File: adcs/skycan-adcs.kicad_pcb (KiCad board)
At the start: 2 copper layers, 50 x 50 mm, 43 parts, among them J1 DF9_25P_1V_PLUG, J2 DF9_25P_1V_SOCKET, J3 DF9_25P_1V_PLUG, J4 DF9_25P_1V_SOCKET, U1 TPS63060, U2 BQ27210, U3 MICRO-B_USB, U4 MCP73831, U5 SWITCH-DPDT

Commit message: adcs routing inprogress
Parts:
- removed BT2: LiPo, PINHEAD1-2
- removed C11, C12: 100nF, SM0402_c
- removed C13, C14: 4.7uF, SM0805
- removed D1: LED, LED-0603
- removed L1: 1uH, COILCRAFT-XFL4020
- removed R10: 2R, SM0402_r
- BT1: value 3x1.5V AAA -> BATTERY; footprint BATTERY-HOLDER-KEYSTONE-2479 -> COINCELL3001; moved to F.Cu
- C1: value 10uF -> 100nF; footprint SM0805 -> SM0402_c
- C10: value 100nF -> 4.7uF; footprint SM0402_c -> SM0603_Capa
- C4: value 10pF -> 100nF
- C5: value 22uF -> 100nF; footprint SM0805 -> SM0402_c
- C6: value 22uF -> 10uF
- C7: value 22uF -> 10uF; footprint SM0805 -> SM0603_Resistor
- C9: value 100nF -> 220nF
- R1, R7: value 1M -> 4.7k
- R2: value 168k -> 4.7k
- R3: value 100k -> 4.7k
- R4: value 1k -> 4.7k
- R5: value 10k -> 330R
- R6: value 1M -> 330R
- R8: value 0.02R -> 4.7k; footprint SM0603_Resistor -> SM0402_r
- R9: value 470R -> 4.7k
- U1: value TPS63060 -> ADT7310; footprint S-PWSON-N10 -> SO8N
- U2: value BQ27210 -> MPL3115A2; footprint S-PVSON-N10 -> LGA8
- U3: value MICRO-B_USB -> LSM303DLHC; footprint MICRO-B_USB -> LGA14L
- U4: value MCP73831 -> MAX-7C; footprint SOT23-5 -> MAX7
- U5: value SWITCH-DPDT -> UFL; footprint MCLSS22P-SWITCH-DPDT -> UFL
- moved R9 45.2 mm to (89.4, 102.5), turned to 180 degrees
- moved G*** 43.4 mm to (168.1, 98.3)
- moved VAL 37.7 mm to (159.8, 79.0)
- moved R8 31.9 mm to (96.1, 102.0), turned to 90 degrees
- moved R7 29.6 mm to (97.3, 102.0), turned to 90 degrees
- moved C5 24.0 mm to (111.8, 100.5)
- moved C1 21.9 mm to (122.0, 107.2), turned to 270 degrees
- moved C6 21.5 mm to (111.9, 102.1)
- moved U3 21.4 mm to (118.7, 117.1), turned to 180 degrees
- moved R3 20.7 mm to (116.8, 110.7), turned to 270 degrees
- moved C3 20.6 mm to (118.7, 103.8), turned to 180 degrees
- moved C2 19.4 mm to (123.8, 107.2), turned to 270 degrees
- moved BT1 17.6 mm to (125.0, 97.4), turned to 0 degrees
- moved R2 15.3 mm to (118.1, 110.7), turned to 270 degrees
- moved U1 14.4 mm to (130.8, 107.1)
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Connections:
- BT1 pad 1: /VBAT -> N-0000022
- BT1 pad 2: GNDPWR -> GND
- C1 pad 1: /VIN -> +3.3V
- C10 pad 1: N-0000010 -> N-0000028
- C10 pad 2: GNDPWR -> GND
- C2 pad 1: /VIN -> +3.3V
- C3 pad 1: N-000008 -> N-0000029
- C4 pad 1: N-0000050 -> +3.3V
- C8 pad 1: N-000009 -> +3.3V
- C8 pad 2: GNDPWR -> GND
- C9 pad 1: N-0000012 -> N-0000026
- C9 pad 2: GNDPWR -> N-0000031
- R1 pad 1: +3.3V -> P1.3
- R1 pad 2: N-0000050 -> +3.3V
- R2 pad 1: N-0000050 -> P1.6
- R2 pad 2: GND -> +3.3V
- R3 pad 1: +3.3V -> P1.7
- R3 pad 2: PGOOD -> +3.3V
- R4 pad 1: N-000009 -> P1.0
- R4 pad 2: /VBAT -> +3.3V
- R5 pad 1: N-0000010 -> N-000004
- R5 pad 2: /VBAT -> RXA1
- R6 pad 1: N-0000052 -> N-000006
- R6 pad 2: GNDPWR -> TXA1
- R7 pad 1: N-0000013 -> P1.5
- R7 pad 2: GND -> +3.3V
- R8 pad 1: GND -> P1.4
- R8 pad 2: GNDPWR -> +3.3V
- R9 pad 1: N-000001 -> P1.2
- R9 pad 2: N-000002 -> +3.3V
- U1 pad 1: N-0000047 -> CLKB1
- U1 pad 2: /VIN -> SOMIB1
- U1 pad 3: /VIN -> SIMOB1
- U1 pad 4: GND -> P4.6
- U1 pad 5: PGOOD -> P1.3
- U1 pad 6: N-000008 -> (no net)
- U1 pad 8: N-0000050 -> +3.3V
- U2 pad 1: N-0000012 -> +3.3V
- U2 pad 2: N-000009 -> N-0000029
- U2 pad 3: GNDPWR -> GND
- U2 pad 4: SCLB0 -> +3.3V
- U2 pad 5: SDAB0 -> P1.7
- U2 pad 6: N-0000010 -> P1.6
- U2 pad 7: N-0000013 -> SDAB0
- U2 pad 8: N-0000052 -> SCLB0
- U3 pad 1: N-000004 -> +3.3V
- U3 pad 2: N-0000029 -> SCLB0
- U3 pad 3: N-0000030 -> SDAB0
- U3 pad 4: N-0000031 -> P1.5
- U3 pad 5: GND -> P1.4
- U4 pad 1: N-000001 -> GND
- U4 pad 2: GND -> N-000004
- U4 pad 3: /VBAT -> N-000006
- U4 pad 4: N-000004 -> P1.1
- U4 pad 5: N-0000028 -> P1.0
- U5 pad 1: /VIN -> N-0000018
- U5 pad 2: /VIN -> GND
- U5 pad 3: /VBAT -> GND
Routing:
- net GND: track 600.8 -> 59.8 mm, vias 274 -> 21
- net +3.3V: track 182.7 -> 66.1 mm
- net GNDPWR: track 69.3 -> 0.00 mm, vias 18 -> 0
- net /VBAT: track 58.2 -> 0.00 mm, vias 2 -> 0
- net P1.1: track 3.01 -> 39.4 mm
- net P1.0: track 3.02 -> 35.2 mm
- net P1.6: track 3.05 -> 31.0 mm
- net P1.7: track 3.04 -> 27.3 mm
- net SCLB0: track 29.8 -> 54.0 mm
- net TXA1: track 2.19 -> 23.4 mm, vias 1 -> 3
- net RXA1: track 2.17 -> 21.5 mm
- net SDAB0: track 32.4 -> 51.3 mm, vias 5 -> 3
- net /VIN: track 16.3 -> 0.00 mm
- net P4.6: track 2.17 -> 18.2 mm
- net N-000004: track 16.5 -> 1.89 mm
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- removed copper zone on F.Cu, net /VBAT
- removed copper zone on B.Cu, net GNDPWR
- removed copper zone on F.Cu, net GNDPWR
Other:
- board text removed: "+"
- board text removed: "-"
- board text removed: "0"
- board text removed: "1"

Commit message: punch of stuff routed in adcs
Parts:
- moved R1 24.6 mm to (103.3, 116.2), turned to 180 degrees
- moved R9 20.3 mm to (103.3, 117.3)
- moved R2 15.0 mm to (103.3, 112.8), turned to 180 degrees
- moved R8 14.9 mm to (103.3, 115.1), turned to 180 degrees
- moved R3 13.6 mm to (103.3, 111.6), turned to 180 degrees
- moved R7 13.3 mm to (103.3, 113.9), turned to 180 degrees
- moved C5 5.74 mm to (116.5, 103.8)
- moved C6 3.81 mm to (115.7, 102.0)
- moved R4 1.40 mm to (125.6, 121.3)
- moved C1 0.65 mm to (122.2, 106.6)
- moved C2 0.13 mm to (124.0, 107.2)
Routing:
- net P1.6: track 31.0 -> 5.48 mm
- net P1.7: track 27.3 -> 6.12 mm
- net P1.0: track 35.2 -> 27.4 mm
- net +3.3V: track 66.1 -> 72.6 mm
- net P1.1: track 39.4 -> 35.6 mm
- net P1.2: track 16.3 -> 18.8 mm
- net P1.3: track 3.09 -> 5.47 mm
- net P1.5: track 15.5 -> 17.9 mm
- net P1.4: track 14.5 -> 16.8 mm
- net N-0000029: track 0.00 -> 1.97 mm
- net N-0000026: track 0.00 -> 1.94 mm
- net N-0000031: track 0.00 -> 1.90 mm

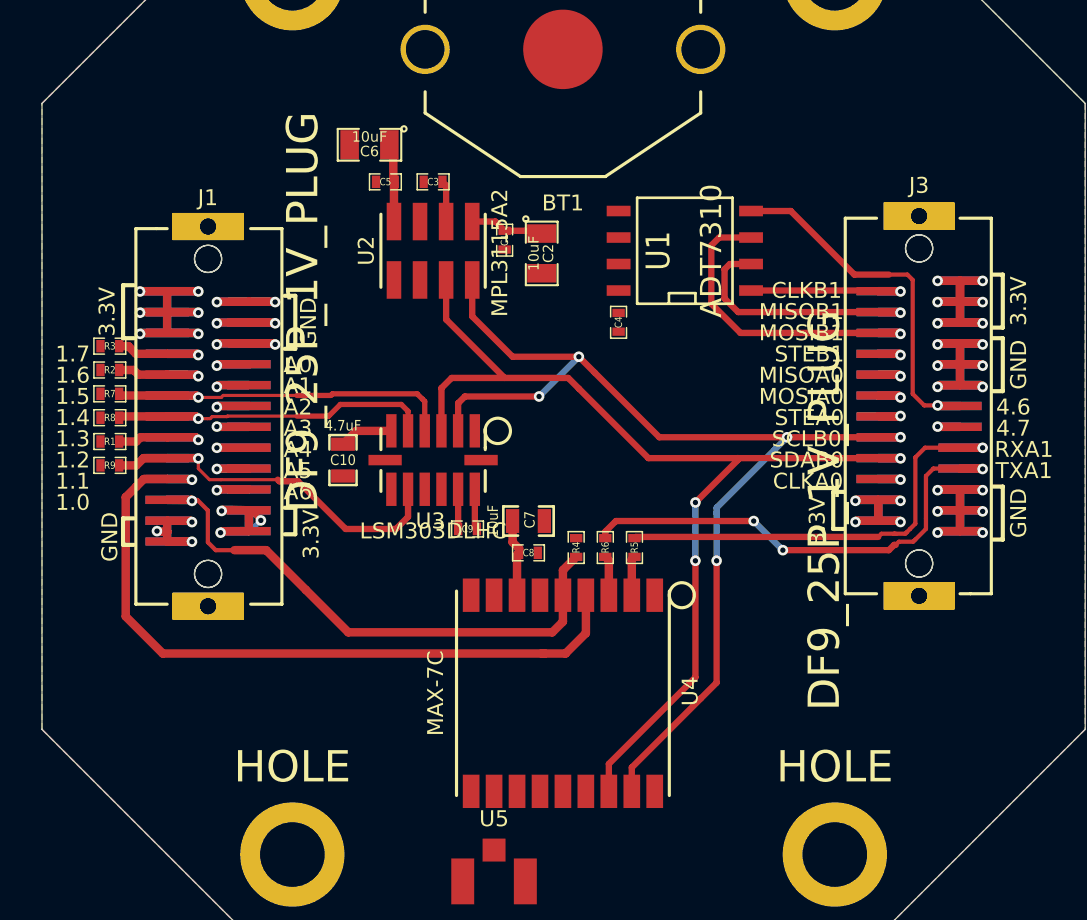
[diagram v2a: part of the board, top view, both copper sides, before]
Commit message: signals routed
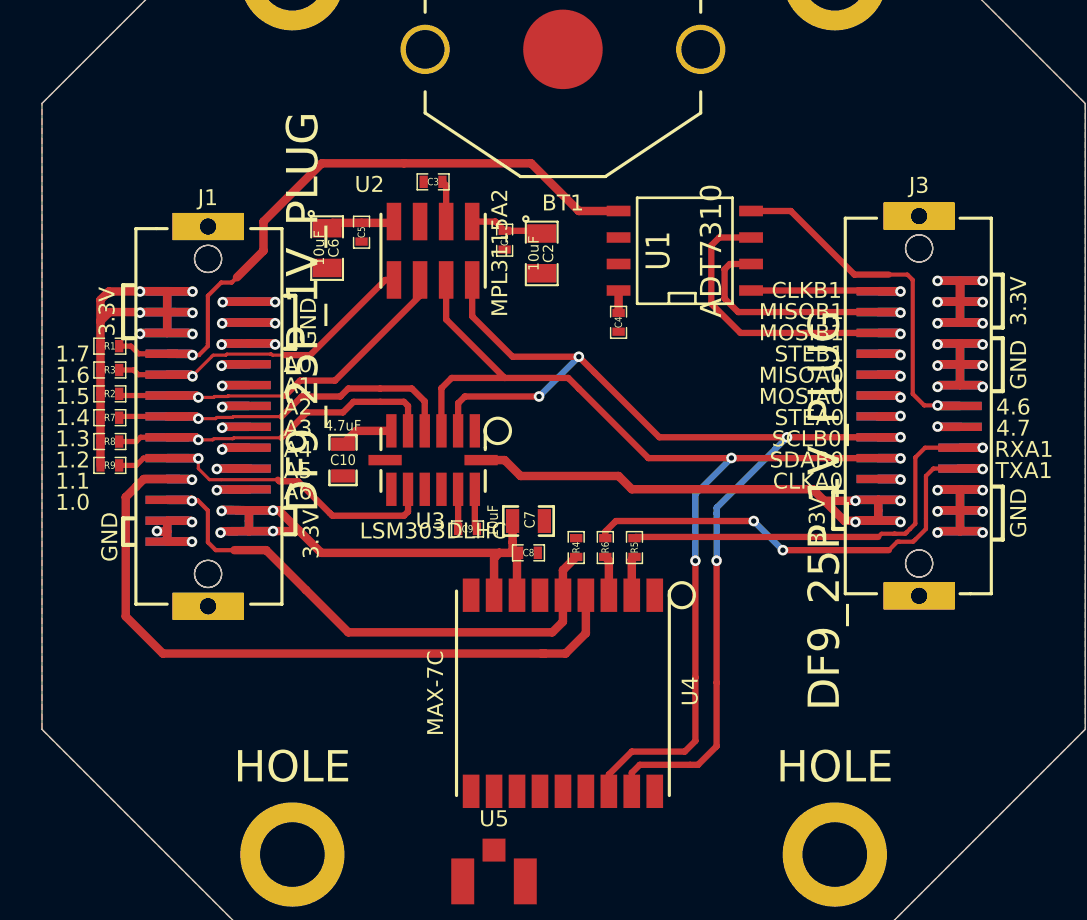
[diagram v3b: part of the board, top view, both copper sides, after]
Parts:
- moved C6 5.35 mm to (113.7, 106.9), turned to 270 degrees
- moved R1 4.57 mm to (103.3, 111.6)
- moved C5 2.67 mm to (115.3, 106.2), turned to 270 degrees
- moved R2 1.14 mm to (103.3, 113.9)
- moved R3 1.14 mm to (103.3, 112.8)
- moved R7 1.14 mm to (103.3, 115.1)
- moved R8 1.14 mm to (103.3, 116.2)
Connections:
- R1 pad 1: P1.3 -> P1.7
- R2 pad 1: P1.6 -> P1.5
- R3 pad 1: P1.7 -> P1.6
- R7 pad 1: P1.5 -> P1.4
- R8 pad 1: P1.4 -> P1.3
- U1 pad 5: P1.3 -> P1.7
- U2 pad 5: P1.7 -> P1.6
- U2 pad 6: P1.6 -> P1.5
- U3 pad 4: P1.5 -> P1.4
- U3 pad 5: P1.4 -> P1.3
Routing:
- net +3.3V: track 72.6 -> 123.9 mm, vias 19 -> 20
- net P1.7: track 6.12 -> 32.4 mm
- net P1.3: track 5.47 -> 17.6 mm
- net P1.6: track 5.48 -> 17.2 mm
- net P1.4: track 16.8 -> 18.5 mm
- net SCLB0: track 54.0 -> 55.7 mm
- net GND: track 59.8 -> 58.2 mm
- net SDAB0: track 51.3 -> 52.7 mm
- net P1.5: track 17.9 -> 18.8 mm
- net P1.2: track 18.8 -> 18.1 mm
- net A1: track 3.15 -> 2.60 mm
- net A2: track 3.12 -> 2.61 mm

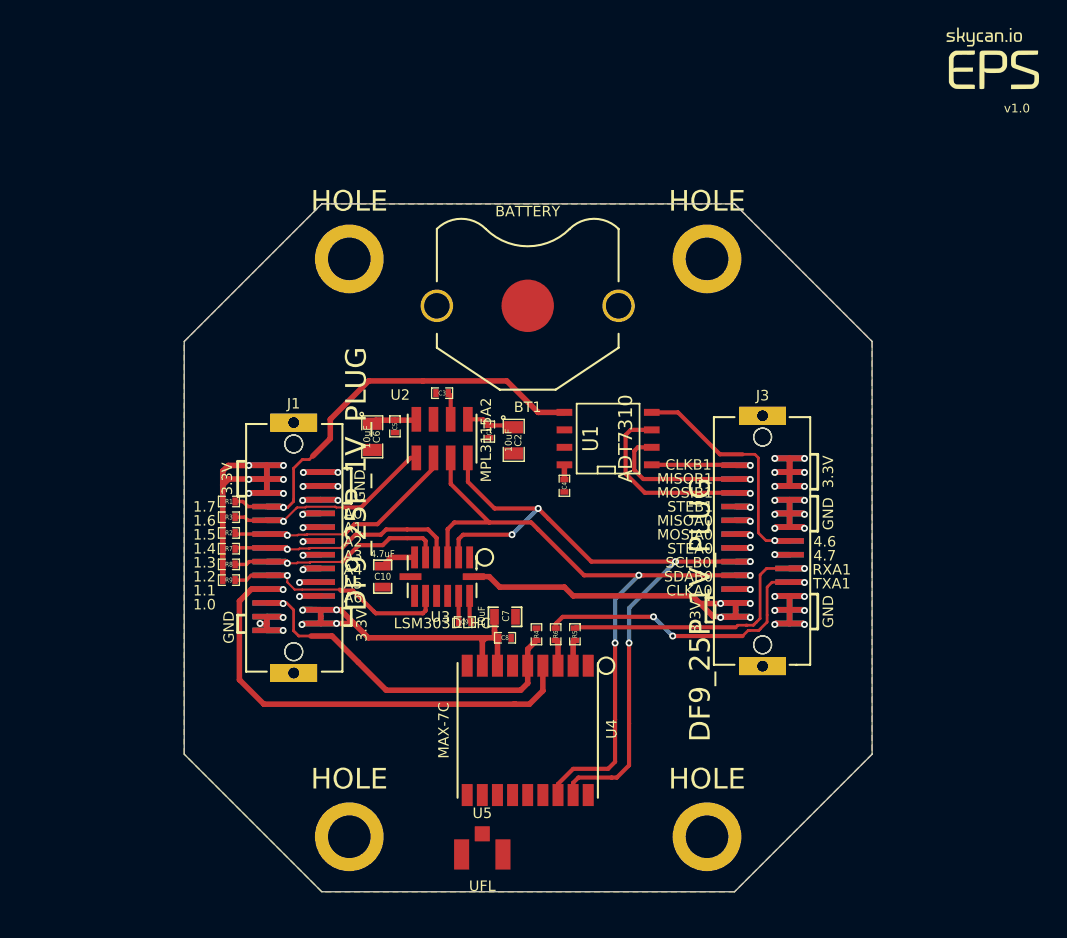
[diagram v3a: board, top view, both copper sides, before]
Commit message: finish adcs routing
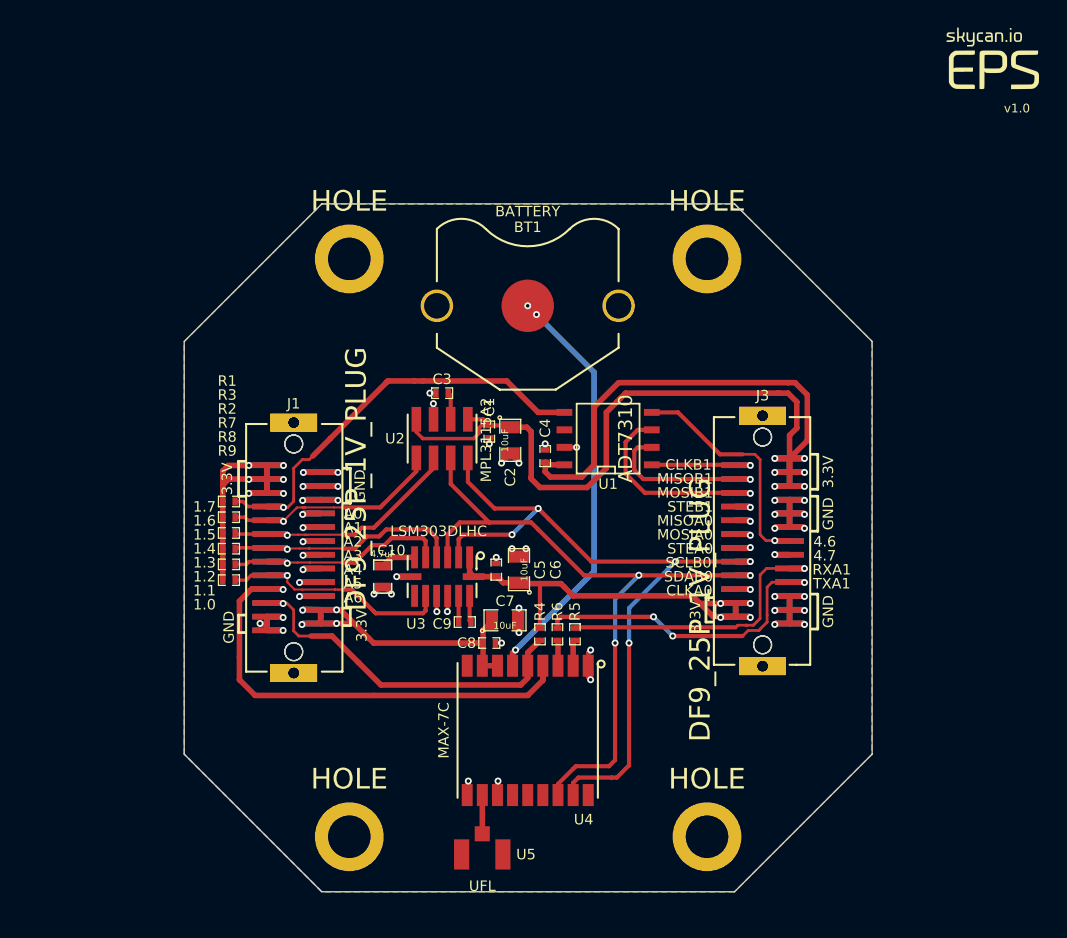
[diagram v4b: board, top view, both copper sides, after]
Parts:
- C7: footprint SM0603_Resistor -> SM0805
- moved C6 14.4 mm to (124.3, 116.6), turned to 90 degrees
- moved C5 12.8 mm to (122.7, 116.6), turned to 90 degrees
- moved C4 2.57 mm to (126.2, 108.3), turned to 90 degrees
- moved C8 1.20 mm to (122.2, 121.9)
- moved C2 0.25 mm to (123.7, 107.2)
- moved C7 0.25 mm to (123.3, 120.3)
- moved R4 0.25 mm to (125.9, 121.3)
- moved R6 0.13 mm to (127.1, 121.3)
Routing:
- net +3.3V: track 123.9 -> 196.2 mm
- net N-0000022: track 0.00 -> 31.5 mm, vias 0 -> 3
- net GND: track 58.2 -> 77.2 mm, vias 21 -> 43
- net N-0000018: track 0.00 -> 2.82 mm
- net P1.1: track 35.6 -> 34.5 mm
- net P1.7: track 32.4 -> 31.6 mm
- net P1.6: track 17.2 -> 17.9 mm

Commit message: finish adcs layout
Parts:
- removed the VAL at (159.8, 79.0)
- added VAL: skycan-adcs-logo, skycan-adcs-logo, F.Cu at (138.9, 127.5)
- moved G*** 46.3 mm to (125.0, 115.0)
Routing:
- net GND: track 77.2 -> 646.8 mm, vias 43 -> 317

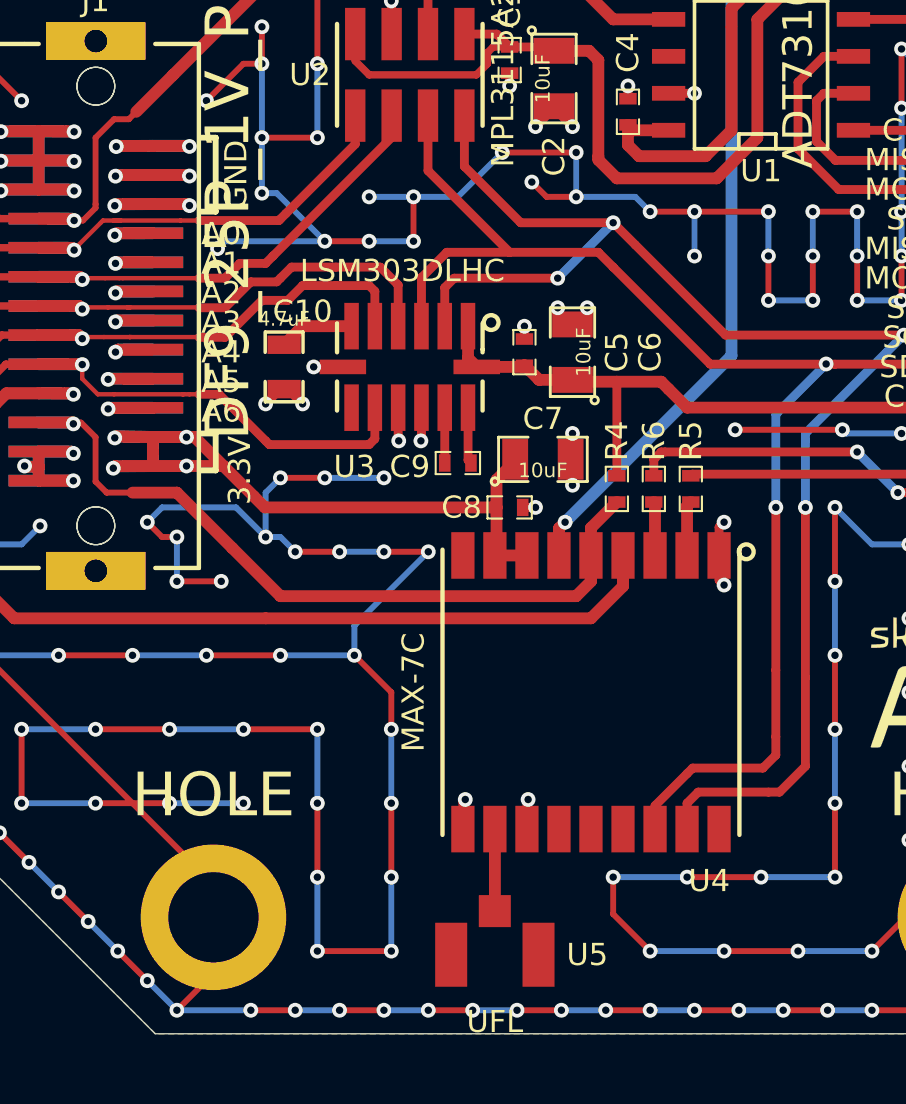
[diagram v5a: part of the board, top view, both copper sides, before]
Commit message: make adcs layout a little nicer
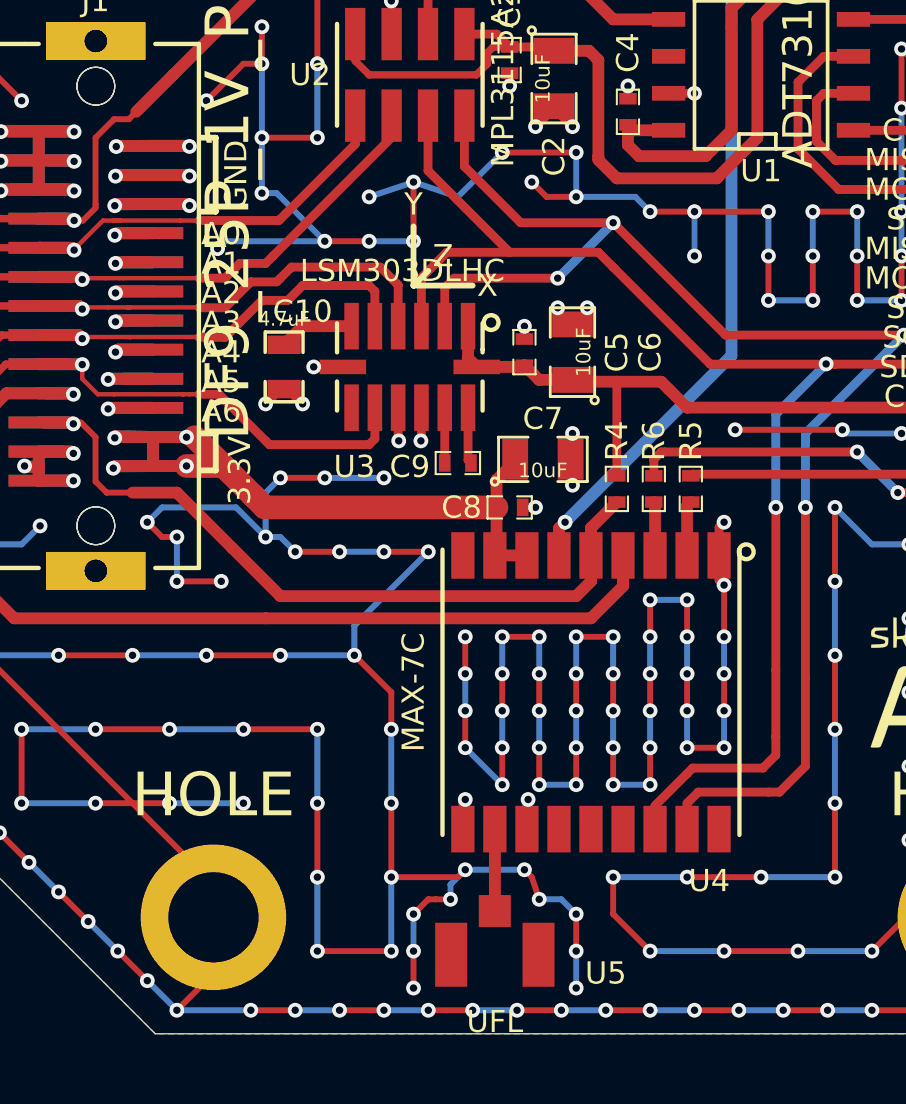
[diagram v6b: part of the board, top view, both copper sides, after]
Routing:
- net GND: track 646.8 -> 713.1 mm, vias 317 -> 366
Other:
- board text added: "X"
- board text added: "Y"
- board text added: "Z"
